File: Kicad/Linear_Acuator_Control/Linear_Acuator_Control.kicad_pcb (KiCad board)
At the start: 2 copper layers, 96.5 x 68 mm, 23 parts, among them K1 RT42xAxx, K3 RT42xAxx, Q1 IRLB3813, Q2 IRLB3813, Q3 2N7002, Q5 2N7002, U1 ESP32-S3-WROOM

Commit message: small stuff
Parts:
- R6: moved to F.Cu
- moved R6 2.50 mm to (128.0, 51.5)
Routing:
- net Net-(Q1-G): track 16.7 -> 19.5 mm, vias 0 -> 1
- net Net-(D3-A): track 127.6 -> 125.3 mm
- net Speed L1: track 58.1 -> 55.8 mm, vias 0 -> 1

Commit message: Updated to SMD comp
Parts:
- removed ?: LOGO, MARS_Footprints:MARS LOGO
- C1, C2: value 1000u -> 1000uF; footprint Capacitor_THT:CP_Radial_D12.5mm_P5.00mm -> Capacitor_THT:CP_Radial_D8.0mm_P3.50mm
- D3, D4: value 1N4148WT -> CD4148WSP; footprint Diode_SMD:D_SOD-523 -> Diode_SMD:D_0805_2012Metric_Pad1.15x1.40mm_HandSolder
- L1: value Linear actuator 1 -> Linear_actuator
- L2: value Linear Actuator 2 -> Linear_actuator
- L3: value 24v 20A Input -> Linear_actuator
- R1, R2, R3, R4: footprint Resistor_THT:R_Axial_DIN0207_L6.3mm_D2.5mm_P10.16mm_Horizontal -> Resistor_SMD:R_0805_2012Metric_Pad1.20x1.40mm_HandSolder
- R5, R6: footprint Resistor_SMD:R_0201_0603Metric -> Resistor_SMD:R_0805_2012Metric_Pad1.20x1.40mm_HandSolder
- U1: footprint PCM_Espressif:ESP32-S3-WROOM-Cam -> Espressif:ESP32-S3-DevKitC
- moved U1 57.8 mm to (87.5, 102.8), turned to 180 degrees
- moved C2 47.6 mm to (132.0, 97.7)
- moved C1 33.0 mm to (100.5, 62.2)
- moved R4 11.6 mm to (80.0, 81.0)
- moved R1 9.29 mm to (79.0, 90.0), turned to 90 degrees
- moved R3 8.46 mm to (72.0, 91.5), turned to 0 degrees
- moved R2 4.45 mm to (73.5, 81.0)
- moved R5 0.50 mm to (94.6, 74.5)
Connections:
- U1 pad 39: Speed L1 -> unconnected-(U1-GPIO42/MTMS-Pad39)
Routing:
- net Net-(D4-A): track 80.9 -> 102.6 mm
- net Net-(D3-A): track 125.3 -> 141.7 mm
- net Dir L2: track 12.6 -> 0.00 mm
- net Net-(Q5-G): track 18.8 -> 10.2 mm
- net GND: track 55.4 -> 49.2 mm
- net +24V: track 188.8 -> 191.8 mm
- net Net-(Q3-G): track 7.95 -> 9.68 mm

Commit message: Final changes before production
Changed some comps and added TVS diodes for overvoltage protection.
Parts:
- added D5: P6KE30CA_C696659, JLCPCB_Circuit_Protection:DO-15_BD3.1-L6.7-P10.70-D0.9-BI, F.Cu at (137.5, 60.5)
- added D6: P6KE30CA_C696659, JLCPCB_Circuit_Protection:DO-15_BD3.1-L6.7-P10.70-D0.9-BI, F.Cu at (133.5, 56.0)
- added G***: LOGO, LOGO, F.Cu at (98.5, 45.0)
- added R7: 10k, Resistor_SMD:R_0805_2012Metric_Pad1.20x1.40mm_HandSolder, F.Cu at (127.0, 77.0)
- added R8: 10k, Resistor_SMD:R_0805_2012Metric_Pad1.20x1.40mm_HandSolder, F.Cu at (96.5, 71.5)
- D3, D4: footprint Diode_SMD:D_0805_2012Metric_Pad1.15x1.40mm_HandSolder -> Diode_SMD:D_0805_2012Metric
- K1: renamed from K3; value RT42xAxx -> RT424024
- K2: renamed from K1; value RT42xAxx -> RT424024
- Q1, Q2: value IRLB3813 -> IRLZ44NPBF
- moved R5 40.8 mm to (128.0, 51.0), turned to -90 degrees
- moved R6 40.6 mm to (94.5, 74.5), turned to 90 degrees
- moved R3 18.2 mm to (69.0, 73.5), turned to -90 degrees
- moved R1 9.30 mm to (71.5, 84.5), turned to 0 degrees
- moved D4 0.39 mm to (118.0, 90.0)
- moved D3 0.20 mm to (136.5, 90.0)
- renumbered L3 to PWD1, Q5 to Q4
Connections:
- R5 pad 1: Speed L2 -> Speed L1
- R5 pad 2: Net-(Q2-G) -> Net-(Q1-G)
- R6 pad 1: Speed L1 -> Speed L2
- R6 pad 2: Net-(Q1-G) -> Net-(Q2-G)
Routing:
- net GND: track 49.2 -> 7.31 mm, vias 27 -> 56
- net Speed L2: track 2.97 -> 34.9 mm
- net Net-(L2-Pin_2): track 23.8 -> 39.1 mm, vias 0 -> 1
- net Dir L2: track 0.00 -> 14.7 mm
- net Speed L1: track 55.8 -> 68.2 mm
- net Dir L1: track 0.00 -> 12.1 mm
- net +24V: track 191.8 -> 180.3 mm
- net Net-(L1-Pin_2): track 24.9 -> 34.0 mm
- net Net-(L2-Pin_1): track 37.1 -> 45.6 mm
- net Net-(Q1-G): track 19.5 -> 27.9 mm, vias 1 -> 0
- net Net-(L1-Pin_1): track 23.1 -> 30.4 mm
- net Net-(Q4-G): track 10.2 -> 15.8 mm
- net Net-(D1-A): track 68.8 -> 63.4 mm
- net Net-(Q3-G): track 9.68 -> 7.68 mm
- net Net-(Q2-G): track 13.5 -> 12.4 mm
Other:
- board text added: "Revision 3"
- board text removed: "36 - Direction L1"
- board text removed: "38 - Speed L2"
- board text removed: "39 - Speed L1"
- board text removed: "47 - Direction L2"
- board text removed: "GND"

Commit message: commit
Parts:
- removed D5, D6: P6KE30CA_C696659, JLCPCB_Circuit_Protection:DO-15_BD3.1-L6.7-P10.70-D0.9-BI
- removed G***: LOGO, LOGO
- removed R7, R8: 10k, Resistor_SMD:R_0805_2012Metric_Pad1.20x1.40mm_HandSolder
- added ?: LOGO, MARS_Footprints:MARS LOGO, F.Cu at (101.7, 43.1)
- C1, C2: value 1000uF -> 1000u; footprint Capacitor_THT:CP_Radial_D8.0mm_P3.50mm -> Capacitor_THT:CP_Radial_D12.5mm_P5.00mm
- D3, D4: value CD4148WSP -> 1N4148WT; footprint Diode_SMD:D_0805_2012Metric -> Diode_SMD:D_SOD-523
- K1: renamed from K2; value RT424024 -> RT42xAxx
- K3: renamed from K1; value RT424024 -> RT42xAxx
- L1: value Linear_actuator -> Linear actuator 1
- L2: value Linear_actuator -> Linear Actuator 2
- L3: renamed from PWD1; value Linear_actuator -> 24v 20A Input
- Q1, Q2: value IRLZ44NPBF -> IRLB3813
- R1, R2, R3, R4: footprint Resistor_SMD:R_0805_2012Metric_Pad1.20x1.40mm_HandSolder -> Resistor_THT:R_Axial_DIN0207_L6.3mm_D2.5mm_P10.16mm_Horizontal
- R5, R6: footprint Resistor_SMD:R_0805_2012Metric_Pad1.20x1.40mm_HandSolder -> Resistor_SMD:R_0201_0603Metric
- U1: footprint Espressif:ESP32-S3-DevKitC -> PCM_Espressif:ESP32-S3-WROOM-Cam
- moved U1 57.8 mm to (79.2, 45.6), turned to 0 degrees
- moved C2 47.6 mm to (100.5, 62.0)
- moved R5 41.1 mm to (94.6, 75.0), turned to 90 degrees
- moved R6 40.6 mm to (128.0, 51.5), turned to -90 degrees
- moved C1 33.0 mm to (133.5, 60.5)
- moved R3 20.4 mm to (80.4, 90.4), turned to 180 degrees
- moved R4 11.6 mm to (70.2, 87.3)
- moved R1 9.62 mm to (80.4, 80.8), turned to 180 degrees
- moved R2 4.45 mm to (70.2, 84.0)
- moved D4 0.39 mm to (118.3, 89.8)
- moved D3 0.20 mm to (136.5, 89.8)
- renumbered Q4 to Q5
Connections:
- R5 pad 1: Speed L1 -> Speed L2
- R5 pad 2: Net-(Q1-G) -> Net-(Q2-G)
- R6 pad 1: Speed L2 -> Speed L1
- R6 pad 2: Net-(Q2-G) -> Net-(Q1-G)
- U1 pad 39: unconnected-(U1-GPIO42/MTMS-Pad39) -> Speed L1
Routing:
- net GND: track 7.31 -> 55.4 mm, vias 56 -> 27
- net Speed L2: track 34.9 -> 2.97 mm
- net Net-(D4-A): track 102.7 -> 80.9 mm
- net Net-(D3-A): track 141.6 -> 125.3 mm
- net Net-(L2-Pin_2): track 39.1 -> 23.8 mm, vias 1 -> 0
- net Speed L1: track 68.2 -> 55.8 mm
- net Dir L1: track 12.1 -> 0.00 mm
- net Net-(L1-Pin_2): track 34.0 -> 24.9 mm
- net +24V: track 180.3 -> 188.8 mm
- net Net-(L2-Pin_1): track 45.6 -> 37.1 mm
- net Net-(Q1-G): track 27.9 -> 19.5 mm, vias 0 -> 1
- net Net-(L1-Pin_1): track 30.4 -> 23.1 mm
- net Net-(D1-A): track 63.4 -> 68.8 mm
- net Net-(Q5-G): track 15.8 -> 18.8 mm
- net Dir L2: track 14.7 -> 12.6 mm
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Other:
- board text added: "36 - Direction L1"
- board text added: "38 - Speed L2"
- board text added: "39 - Speed L1"
- board text added: "47 - Direction L2"
- board text added: "GND"
- board text removed: "Revision 3"

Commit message: rearranging tracks for solder busses
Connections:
- net Net-(D1-A) renamed L1SwitchedLow
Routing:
- net +24V: track 188.8 -> 186.9 mm
- net GND: track 55.4 -> 56.5 mm

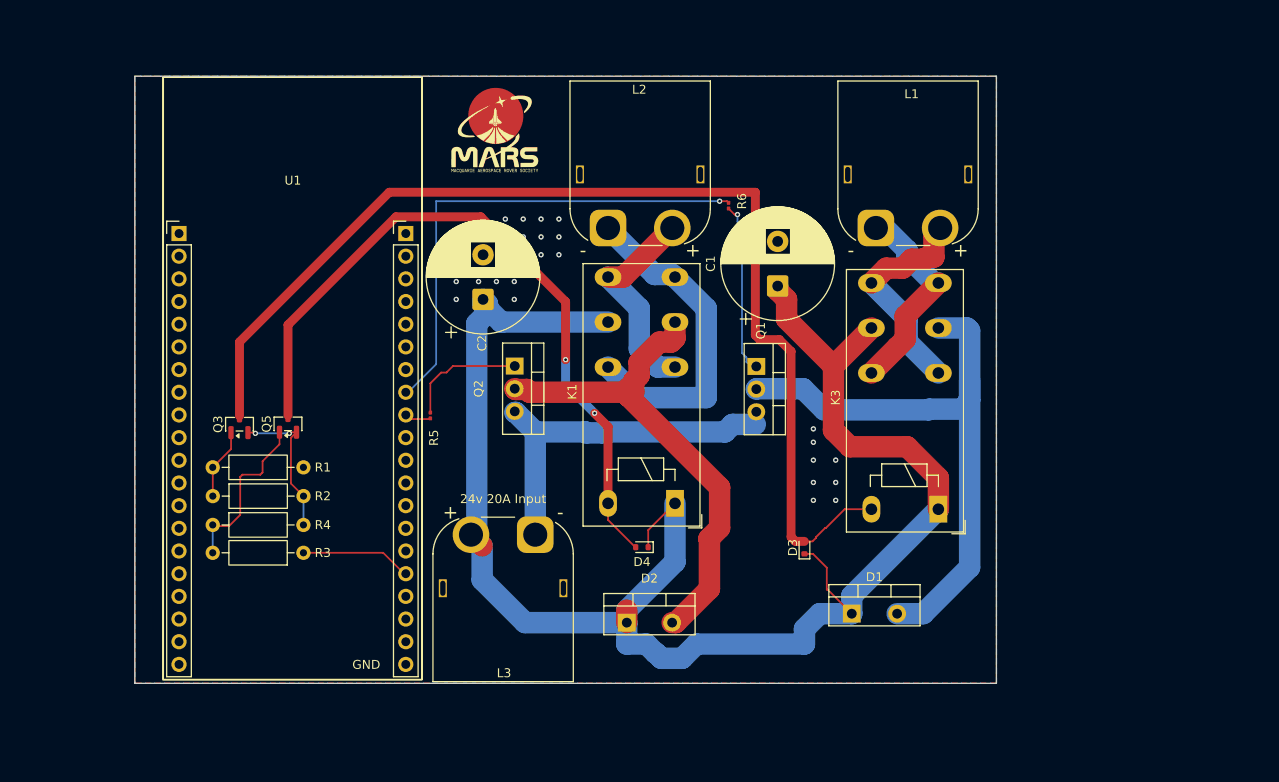
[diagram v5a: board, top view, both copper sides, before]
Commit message: adding part numbers
for some reason the diodes dont work properly with lcsc idk will investigate
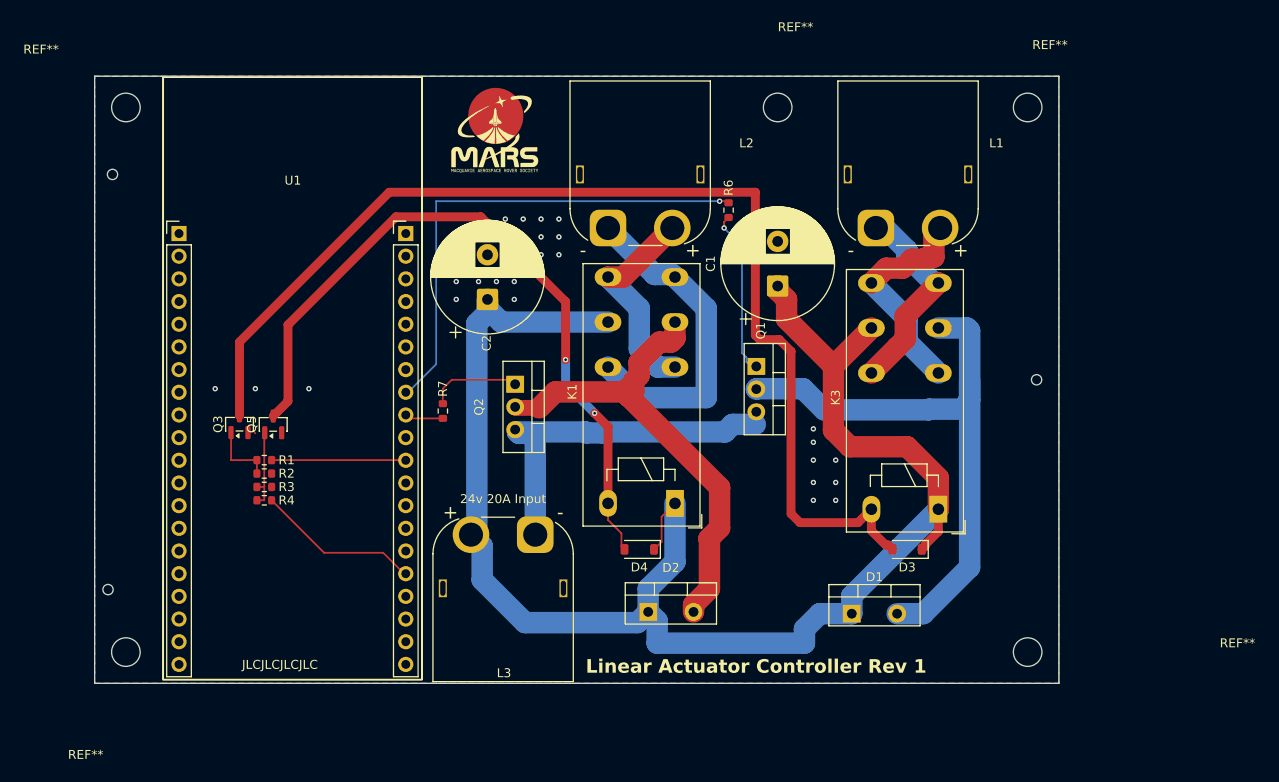
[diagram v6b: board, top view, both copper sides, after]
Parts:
- removed R5: 220, Resistor_SMD:R_0201_0603Metric
- added R7: 220, Resistor_SMD:R_0603_1608Metric, F.Cu at (96.0, 74.5)
- added REF**: ToolingHole_1.152mm, MountingHole:ToolingHole_1.152mm, F.Cu at (162.5, 71.0)
- added REF**: MountingHole_3.2mm_M3, MountingHole:MountingHole_3.2mm_M3, F.Cu at (60.5, 101.5)
- added REF**: MountingHole_3.2mm_M3, MountingHole:MountingHole_3.2mm_M3, F.Cu at (60.5, 40.5)
- added REF**: ToolingHole_1.152mm, MountingHole:ToolingHole_1.152mm, F.Cu at (59.0, 48.0)
- added REF**: MountingHole_3.2mm_M3, MountingHole:MountingHole_3.2mm_M3, F.Cu at (161.5, 101.5)
- added REF**: MountingHole_3.2mm_M3, MountingHole:MountingHole_3.2mm_M3, F.Cu at (133.5, 40.5)
- added REF**: MountingHole_3.2mm_M3, MountingHole:MountingHole_3.2mm_M3, F.Cu at (161.5, 40.5)
- added REF**: ToolingHole_1.152mm, MountingHole:ToolingHole_1.152mm, F.Cu at (58.5, 94.5)
- D3, D4: value 1N4148WT -> 1N4148W; footprint Diode_SMD:D_SOD-523 -> Diode_SMD:D_SOD-123
- R1, R2: footprint Resistor_THT:R_Axial_DIN0207_L6.3mm_D2.5mm_P10.16mm_Horizontal -> Resistor_SMD:R_0603_1608Metric
- R3: value 1k -> 10k; footprint Resistor_THT:R_Axial_DIN0207_L6.3mm_D2.5mm_P10.16mm_Horizontal -> Resistor_SMD:R_0603_1608Metric
- R4: value 10k -> 1k; footprint Resistor_THT:R_Axial_DIN0207_L6.3mm_D2.5mm_P10.16mm_Horizontal -> Resistor_SMD:R_0603_1608Metric
- R6: footprint Resistor_SMD:R_0201_0603Metric -> Resistor_SMD:R_0603_1608Metric
- moved D3 11.5 mm to (148.0, 90.0), turned to 180 degrees
- moved R3 8.58 mm to (76.0, 83.0), turned to 0 degrees
- moved R4 6.40 mm to (76.0, 84.5)
- moved R2 6.30 mm to (76.0, 81.5)
- moved R1 4.46 mm to (76.0, 80.0), turned to 0 degrees
- moved D2 2.68 mm to (119.0, 97.0)
- moved Q2 2.04 mm to (104.1, 71.5)
- moved Q5 1.66 mm to (77.0, 76.0)
- moved C2 0.50 mm to (101.0, 62.0)
- moved R6 0.50 mm to (128.0, 52.0), turned to 90 degrees
- moved D4 0.39 mm to (118.0, 90.0)
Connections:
- R1 pad 1: Dir L1 -> Net-(Q3-G)
- R1 pad 2: Net-(Q3-G) -> Dir L1
- R3 pad 1: Dir L2 -> Net-(Q5-G)
- R3 pad 2: Net-(Q5-G) -> GND
- R4 pad 2: GND -> Dir L2
- R6 pad 1: Speed L1 -> Net-(Q1-G)
- R6 pad 2: Net-(Q1-G) -> Speed L1
- U1 pad 36: unconnected-(U1-GPIO39/MTCK-Pad36) -> Dir L1
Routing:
- net GND: track 56.5 -> 40.8 mm, vias 27 -> 28
- net Dir L1: track 0.00 -> 15.0 mm
- net Net-(Q5-G): track 18.8 -> 9.23 mm
- net +24V: track 186.9 -> 179.7 mm
- net Dir L2: track 12.6 -> 18.6 mm
- net Net-(Q2-G): track 13.5 -> 10.4 mm
- net Net-(D3-A): track 125.3 -> 127.6 mm
- net Speed L2: track 2.97 -> 4.96 mm
- net Net-(D2-A): track 57.2 -> 55.3 mm
- net Net-(Q1-G): track 19.5 -> 18.7 mm
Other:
- board size 96.5 x 68 mm -> 108 x 68 mm
- board text added: "JLCJLCJLCJLC"
- board text added: "Linear Actuator Controller Rev 1"
